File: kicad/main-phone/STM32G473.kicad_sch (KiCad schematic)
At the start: 34 parts, among them J7301 SPARE-IO (DNP), T1 NTCG164KF104FT1, U13 STM32G473VCT6, X1 ABM3-8_000MHZ-D2Y-T, X3 XKXEL89CII-SUAYLC-32_768K

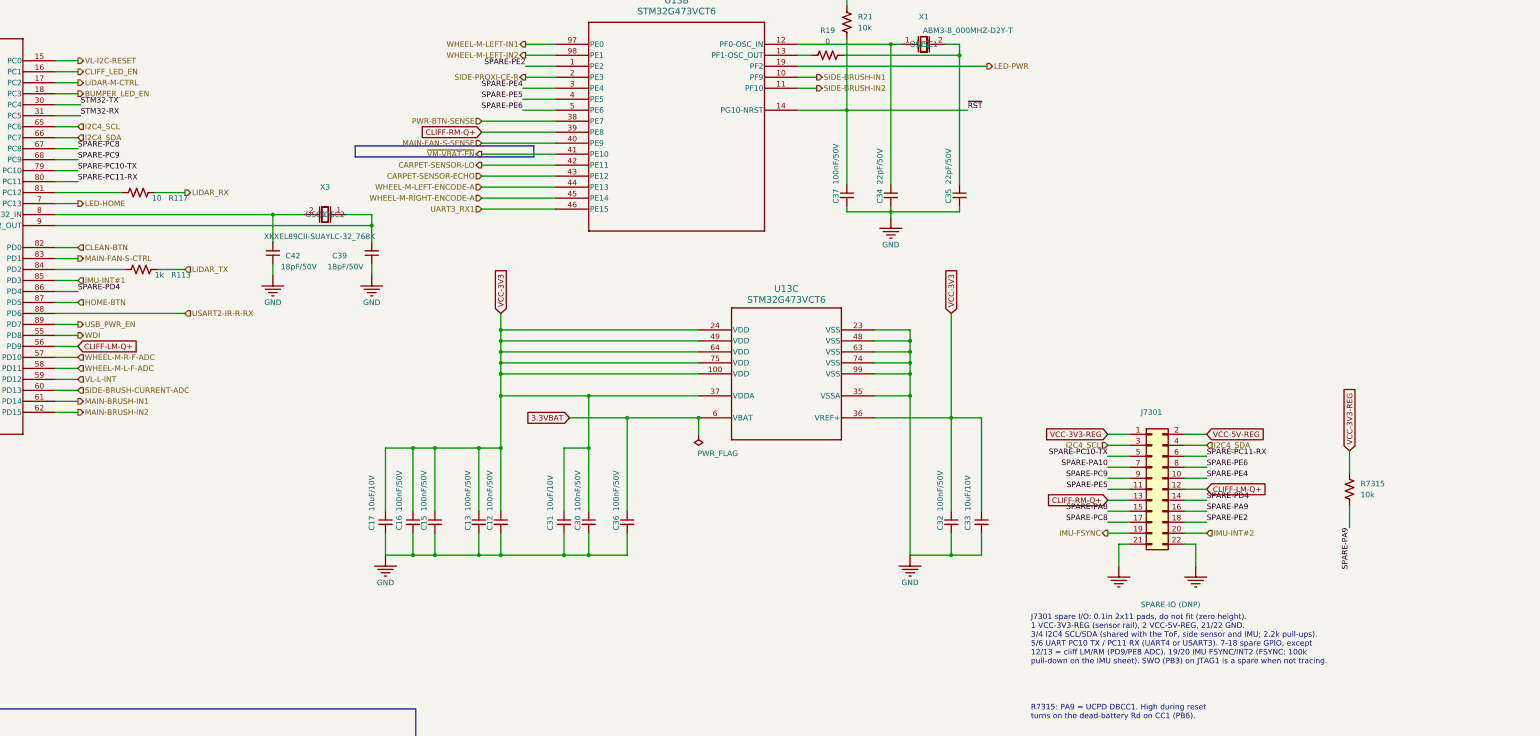
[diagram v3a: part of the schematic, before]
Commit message: Rear docking IR board and Hall sensor board; main-board connectors
- kicad/rear-ir: 2x top-looking IRM-H638T with per-receiver 100R + 10uF filters, SH 4-pin
  vertical (3.3 V, IR_L, IR_R, GND), 2x M2. Refs 86xx.
- kicad/hall-sensor: CC6201ST omnipolar Hall switch + 100 nF, SH 4-pin vertical, 2x M2;
  fitted twice (dust bin, LiDAR tower bumper). Refs 87xx.
- main-phone SIDE-PROXI sheet: REAR-IR1 (PC8/PC9), HALL-BIN1 (PE4), HALL-TOWER1 (PE5),
  47k Hall pull-ups R7801/R7802; global labels to the MCU sheet; J7301 labels updated
- JLCImport: CC6201ST
- docs: board READMEs, SPEC, READMEs

Co-Authored-By: Claude Opus 5.5 <noreply@anthropic.com>
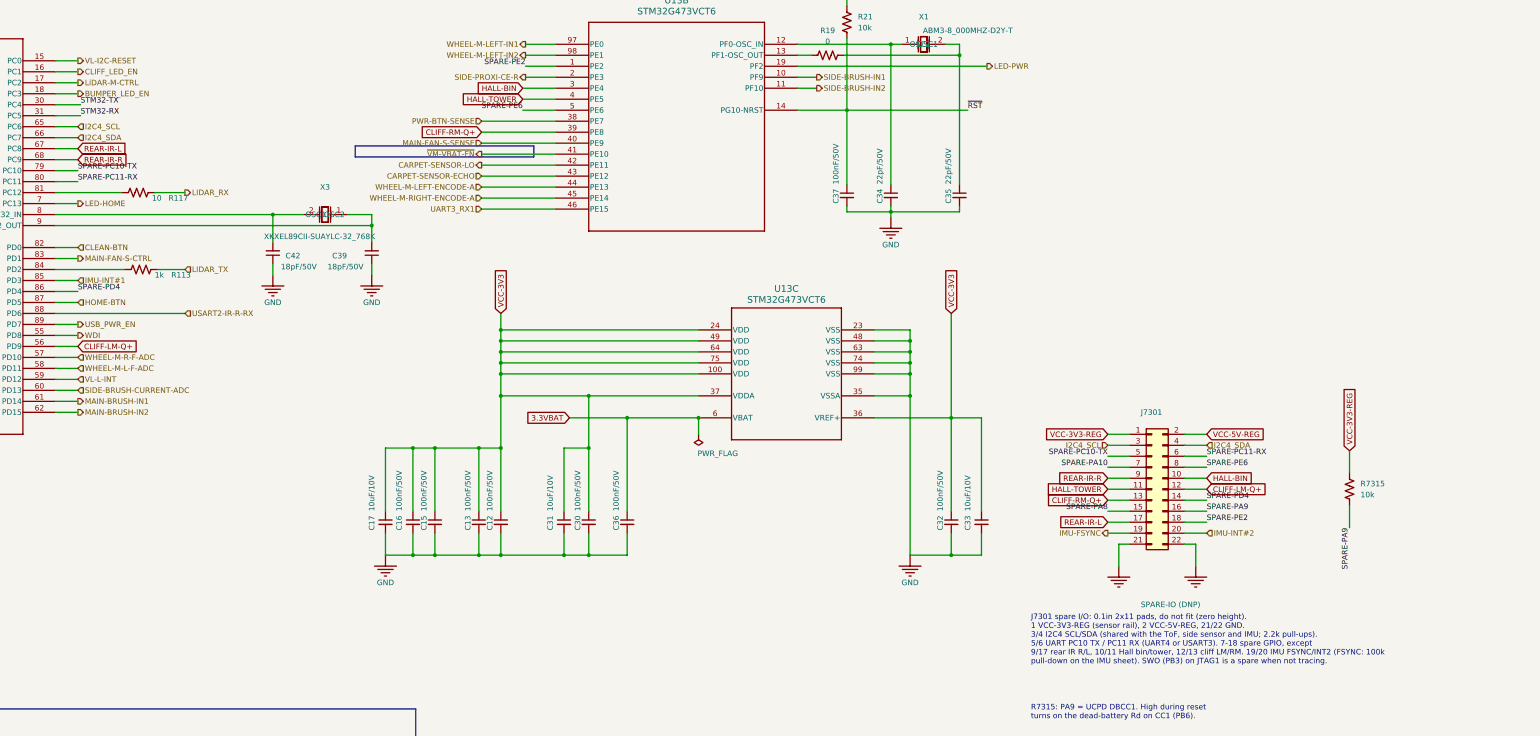
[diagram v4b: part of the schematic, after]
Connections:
- net SPARE-PC8 renamed REAR-IR-L
- net SPARE-PC9 renamed REAR-IR-R
- net SPARE-PE4 renamed HALL-BIN
- net SPARE-PE5 renamed HALL-TOWER
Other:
- note added: "J7301 spare I/O: 0.1in 2x11 pads, do not fit (zero height). 1 VCC-3V3-REG (sensor rail), 2 VCC-5V-REG, 21/22 GND. 3/4 I2C4 SCL/SDA (shared with the ToF, side sensor and IMU; 2.2k pull-ups). 5/6 UART PC10 TX / PC11 RX (UART4 or USART3). 7-18 spare GPIO, except 9/17 rear IR R/L, 10/11 Hall bin/tower, 12/13 cliff LM/RM. 19/20 IMU FSYNC/INT2 (FSYNC: 100k pull-down on the IMU sheet). SWO (PB3) on JTAG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"
- note removed: "J7301 spare I/O: 0.1in 2x11 pads, do not fit (zero height). 1 VCC-3V3-REG (sensor rail), 2 VCC-5V-REG, 21/22 GND. 3/4 I2C4 SCL/SDA (shared with the ToF, side sensor and IMU; 2.2k pull-ups). 5/6 UART PC10 TX / PC11 RX (UART4 or USART3). 7-18 spare GPIO, except 12/13 = cliff LM/RM (PD9/PE8 ADC). 19/20 IMU FSYNC/INT2 (FSYNC: 100k pull-down on the IMU sheet). SWO (PB3) on JTAG1 is a spare when not tr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"
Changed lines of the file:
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@@
 		)
 	)
-	(label "SPARE-PC8"
+	(global_label "REAR-IR-L"
+		(shape input)
 		(at 272.415 116.84 0)
+		(fields_autoplaced yes)
 		(effects
 			(font
 				(size 1.27 1.27)
 			)
-			(justify left bottom)
+			(justify left)
+		)
+		(property "Intersheetrefs" "${INTERSHEET_REFS}"
+			(at 272.415 116.84 0)
+			(hide yes)
+			(show_name no)
+			(do_not_autoplace no)
+			(effects
+				(font
+					(size 1.27 1.27)
+				)
+				(justify left)
+			)
 		)
 	)
@@
 		)
 	)
-	(label "SPARE-PC9"
+	(global_label "REAR-IR-R"
+		(shape input)
 		(at 272.415 119.38 0)
+		(fields_autoplaced yes)
 		(effects
 			(font
 				(size 1.27 1.27)
 			)
-			(justify left bottom)
+			(justify left)
+		)
+		(property "Intersheetrefs" "${INTERSHEET_REFS}"
+			(at 272.415 119.38 0)
+			(hide yes)
+			(show_name no)
+			(do_not_autoplace no)
+			(effects
+				(font
+					(size 1.27 1.27)
+				)
+				(justify left)
+			)
 		)
 	)
@@
 		)
 	)
-	(label "SPARE-PE4"
+	(global_label "HALL-BIN"
+		(shape input)
 		(at 375.285 102.87 180)
+		(fields_autoplaced yes)
 		(effects
 			(font
 				(size 1.27 1.27)
 			)
-			(justify right bottom)
+			(justify right)
+		)
+		(property "Intersheetrefs" "${INTERSHEET_REFS}"
+			(at 375.285 102.87 180)
+			(hide yes)
+			(show_name no)
+			(do_not_autoplace no)
+			(effects
+				(font
+					(size 1.27 1.27)
+				)
+				(justify right)
+			)
 		)
 	)
@@
 		)
 	)
-	(label "SPARE-PE5"
+	(global_label "HALL-TOWER"
+		(shape input)
 		(at 375.285 105.41 180)
+		(fields_autoplaced yes)
 		(effects
 			(font
 				(size 1.27 1.27)
 			)
-			(justify right bottom)
+			(justify right)
+		)
+		(property "Intersheetrefs" "${INTERSHEET_REFS}"
+			(at 375.285 105.41 180)
+			(hide yes)
+			(show_name no)
+			(do_not_autoplace no)
+			(effects
+				(font
+					(size 1.27 1.27)
+				)
+				(justify right)
+			)
 		)
 	)
@@
 		)
 	)
-	(label "SPARE-PC9"
+	(global_label "REAR-IR-R"
+		(shape input)
 		(at 510.54 193.04 180)
+		(fields_autoplaced yes)
 		(effects
 			(font
 				(size 1.27 1.27)
 			)
-			(justify right bottom)
+			(justify right)
+		)
+		(property "Intersheetrefs" "${INTERSHEET_REFS}"
+			(at 510.54 193.04 180)
+			(hide yes)
+			(show_name no)
+			(do_not_autoplace no)
+			(effects
+				(font
+					(size 1.27 1.27)
+				)
+				(justify right)
+			)
 		)
 	)
@@
 		)
 	)
-	(label "SPARE-PE4"
+	(global_label "HALL-BIN"
+		(shape input)
 		(at 533.4 193.04 0)
+		(fields_autoplaced yes)
 		(effects
 			(font
 				(size 1.27 1.27)
 			)
-			(justify left bottom)
+			(justify left)
+		)
+		(property "Intersheetrefs" "${INTERSHEET_REFS}"
+			(at 533.4 193.04 0)
+			(hide yes)
+			(show_name no)
+			(do_not_autoplace no)
+			(effects
+				(font
+					(size 1.27 1.27)
+				)
+				(justify left)
+			)
 		)
 	)
@@
 		)
 	)
-	(label "SPARE-PE5"
+	(global_label "HALL-TOWER"
+		(shape input)
 		(at 510.54 195.58 180)
+		(fields_autoplaced yes)
 		(effects
 			(font
 				(size 1.27 1.27)
 			)
-			(justify right bottom)
+			(justify right)
+		)
+		(property "Intersheetrefs" "${INTERSHEET_REFS}"
+			(at 510.54 195.58 180)
+			(hide yes)
+			(show_name no)
+			(do_not_autoplace no)
+			(effects
+				(font
+					(size 1.27 1.27)
+				)
+				(justify right)
+			)
 		)
 	)
@@
 		)
 	)
-	(label "SPARE-PC8"
+	(global_label "REAR-IR-L"
+		(shape input)
 		(at 510.54 203.2 180)
+		(fields_autoplaced yes)
 		(effects
 			(font
 				(size 1.27 1.27)
 			)
-			(justify right bottom)
+			(justify right)
+		)
+		(property "Intersheetrefs" "${INTERSHEET_REFS}"
+			(at 510.54 203.2 180)
+			(hide yes)
+			(show_name no)
+			(do_not_autoplace no)
+			(effects
+				(font
+					(size 1.27 1.27)
+				)
+				(justify right)
+			)
 		)
 	)
@@
 		)
 	)
-	(text "J7301 spare I/O: 0.1in 2x11 pads, do not fit (zero height).\n1 VCC-3V3-REG (sensor rail), 2 VCC-5V-REG, 21/22 GND.\n3/4 I2C4 SCL/SDA (shared with the ToF, side sensor and IMU; 2.2k pull-ups).\n5/6 UART PC10 TX / PC11 RX (UART4 or USART3). 7-18 spare GPIO, except\n12/13 = cliff LM/RM (PD9/PE8 ADC). 19/20 IMU FSYNC/INT2 (FSYNC: 100k\npull-down on the IMU sheet). SWO (PB3) on JTAG1 is a spare when not tracing."
+	(text "J7301 spare I/O: 0.1in 2x11 pads, do not fit (zero height).\n1 VCC-3V3-REG (sensor rail), 2 VCC-5V-REG, 21/22 GND.\n3/4 I2C4 SCL/SDA (shared with the ToF, side sensor and IMU; 2.2k pull-ups).\n5/6 UART PC10 TX / PC11 RX (UART4 or USART3). 7-18 spare GPIO, except\n9/17 rear IR R/L, 10/11 Hall bin/tower, 12/13 cliff LM/RM. 19/20 IMU FSYNC/INT2 (FSYNC: 100k\npull-down on the IMU sheet). SWO (PB3) on JTAG1 is a spare when not tracing."
 		(exclude_from_sim no)
 		(at 492.76 236.22 0)
